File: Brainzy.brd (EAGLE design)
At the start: 100 x 80 mm, 46 parts, among them IC1 L293D, IC2 L293D

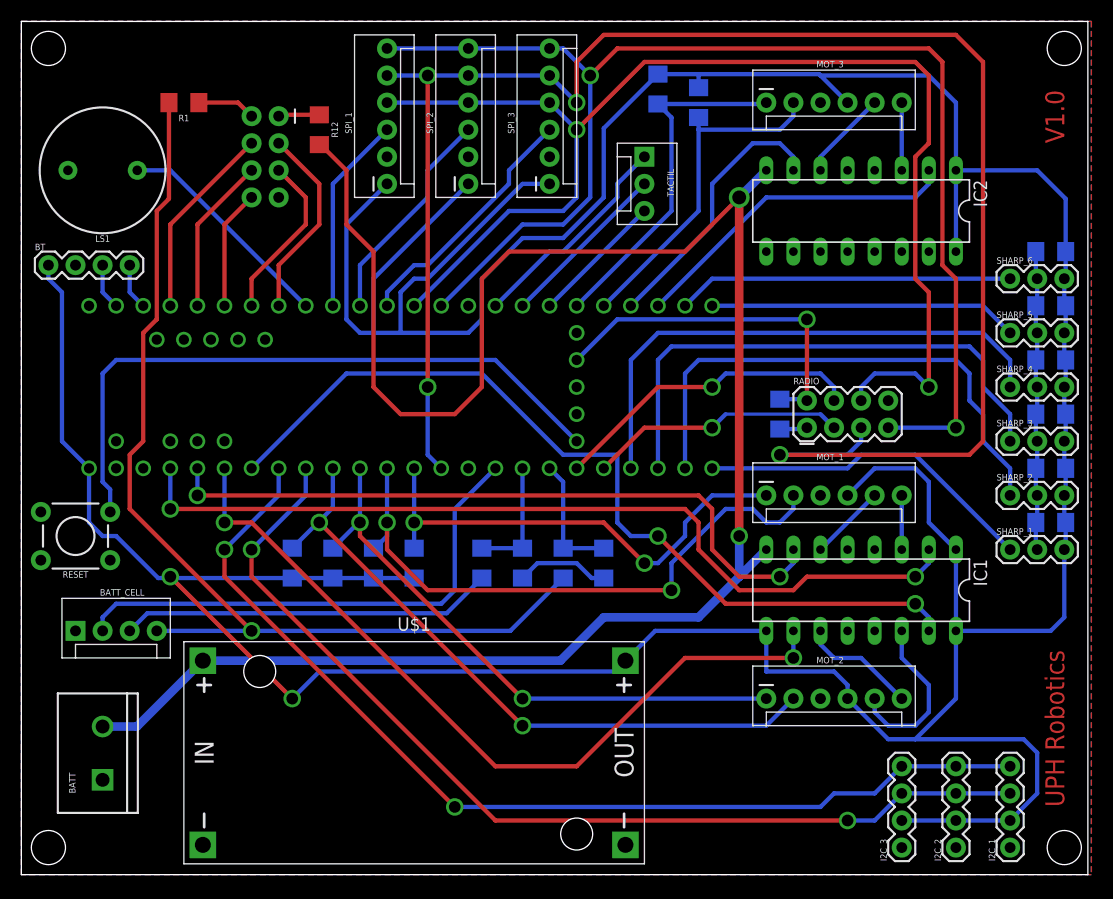
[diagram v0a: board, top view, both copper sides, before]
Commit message: Upload Brainzy v1.1
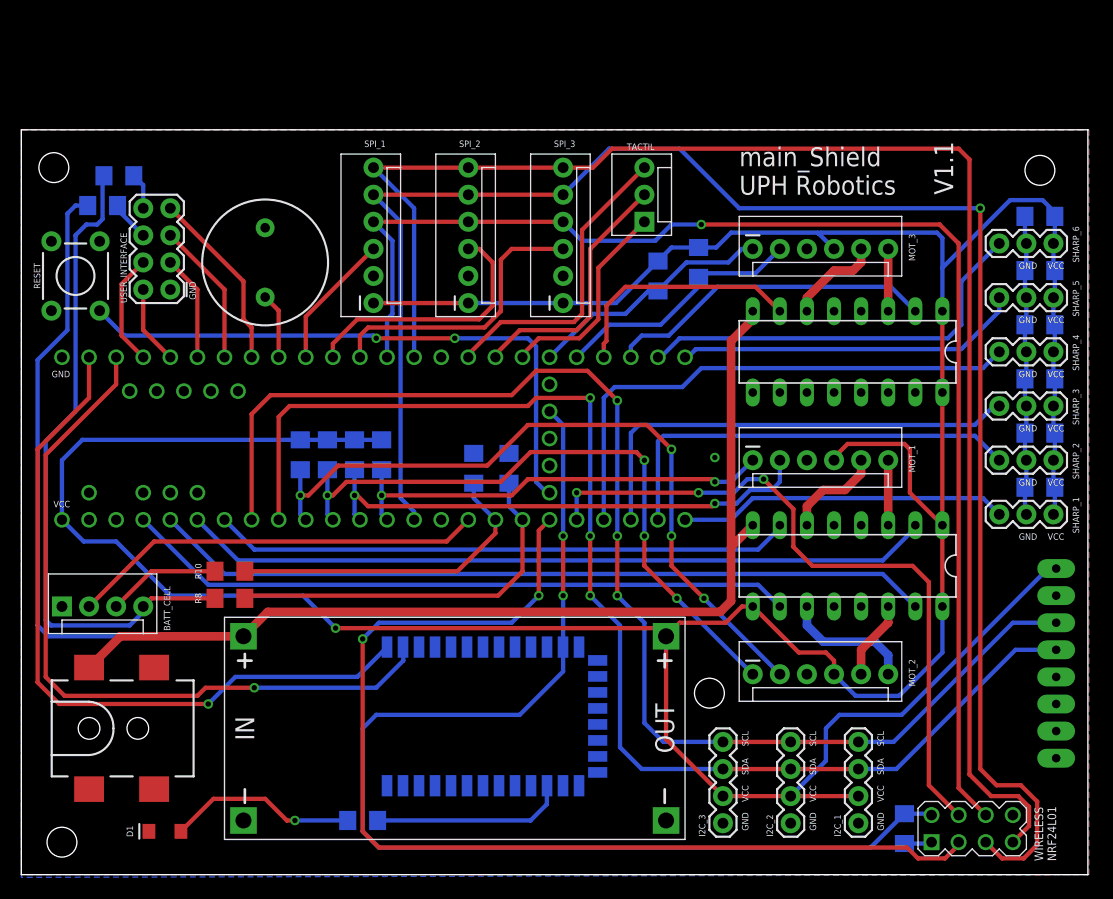
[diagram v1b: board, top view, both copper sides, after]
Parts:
- removed IU, RADIO: (no value), SparkFun-Connectors:2X4
- removed U$1: DC-DC-STEP-DOWN-LM2596, DC-DC-STEP-DOWN-LM2596:DC-DC-STEP-DOWN-LM2596
- added D1: (no value), SparkFun-LED:LED-1206
- added M1: WIRELESS-NRF24L01, diy-modules copy:WIRELESS-NRF24L01
- added POWER_CONVERTER: DC-DC-STEP-DOWN-LM2596, diy-modules copy:DC-DC-STEP-DOWN-LM2596
- added R13: 470, SparkFun-Resistors:1206
- added U1: GY-521MPU6050, gy-521:GY-521
- added USER_INTERFACE: (no value), SparkFun-Connectors:2X4
- BATT: value (none) -> 5.5x2.1mm Barrel; device SparkFun-Connectors:SCREWTERMINAL-5MM-2 -> SparkFun-Connectors:POWER_JACK_SMD
- BT: value (none) -> HC-06/HC_05; device SparkFun-Connectors:1X04 -> SerialPortBluetooth:BLUETOOTH_SMD
- TEENSY_3.2/3.5: value TEENSY_3.5_ALL_PINS -> TEENSY_ALL_PINS
- moved BT 47.9 mm to (34.3, 21.3), flipped to the bottom, turned to 270 degrees
- moved C1 40.6 mm to (82.8, 4.32), turned to 270 degrees
- moved R8 31.4 mm to (19.6, 25.9), flipped to the top, turned to 180 degrees
- moved RESET 24.4 mm to (5.08, 56.1), turned to 90 degrees
- moved R10 23.6 mm to (19.6, 28.4), flipped to the top, turned to 180 degrees
- moved R12 21.5 mm to (7.62, 62.7), flipped to the bottom, turned to 0 degrees
- moved R7 17.5 mm to (59.7, 56.1)
- moved LS1 17.5 mm to (22.9, 57.4), turned to 90 degrees
- moved I2C_3 16.9 mm to (65.8, 4.83)
- moved I2C_2 15.7 mm to (72.1, 4.83)
- moved R6 15.0 mm to (63.5, 57.4)
- moved I2C_1 14.4 mm to (78.5, 4.83)
- moved MOT_3 13.8 mm to (68.6, 58.7)
- moved IC2 13.3 mm to (77.5, 49.0)
- moved R9 12.6 mm to (45.7, 38.1), turned to 270 degrees
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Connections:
- removed net N$2: IU.2, R1.1
- new net N$3: D1.A, R13.1
- new net N$4: R12.1, USER_INTERFACE.6
- new net N$6: BT.24, R13.2
- net 12V: now also BATT.VIN0, POWER_CONVERTER.IN+; no longer BATT.2, U$1.IN+
- net 3.3V: now also BT.12, C1.1, M1.2; no longer C1.2, RADIO.2
- net 5V: now also POWER_CONVERTER.OUT+, U1.VCC; no longer BT.1, U$1.OUT+
- net BTN_CENTER: now also USER_INTERFACE.3; no longer IU.8
- net BTN_DOWN: now also USER_INTERFACE.7; no longer IU.3
- net BTN_LEFT: now also USER_INTERFACE.2; no longer IU.6
- net BTN_RIGHT: now also USER_INTERFACE.5; no longer IU.5
- net BTN_UP: now also USER_INTERFACE.4; no longer IU.4
- net BT_RX: now also BT.1; no longer BT.3
- net BT_TX: now also BT.2; no longer BT.4
- net GND: now also BATT.GND, BT.13, BT.21, BT.22, C1.2, D1.C, M1.1, POWER_CONVERTER.IN-, POWER_CONVERTER.OUT-, U1.GND, USER_INTERFACE.1; no longer BATT.1, BT.2, C1.1, IU.7, RADIO.1, U$1.IN-, U$1.OUT-
- net MOT1_1: now also TEENSY_3.2/3.5.21/A7; no longer TEENSY_3.2/3.5.23/A9
- net MOT1_2: now also TEENSY_3.2/3.5.20/A6; no longer TEENSY_3.2/3.5.22/A8
- net MOT2_1: now also TEENSY_3.2/3.5.23/A9; no longer TEENSY_3.2/3.5.21/A7
- net MOT2_2: now also TEENSY_3.2/3.5.22/A8; no longer TEENSY_3.2/3.5.20/A6
- net N$1: now also R1.1, USER_INTERFACE.8; no longer IU.1, R12.1
- net RADIO_CE: now also M1.3, TEENSY_3.2/3.5.38/A19; no longer RADIO.3, TEENSY_3.2/3.5.37/A18
- net RADIO_CS: now also M1.4, TEENSY_3.2/3.5.37/A18; no longer RADIO.4, TEENSY_3.2/3.5.38/A19
- net SCL: now also U1.SCL
- net SDA: now also U1.SDA
- net SPI_MISO: now also M1.7; no longer RADIO.7
- net SPI_MOSI: now also M1.6; no longer RADIO.6
- net SPI_SCK: now also M1.5; no longer RADIO.5
- net T_CS2: now also TACTIL.1; no longer TACTIL.3
- net T_IRQ: now also TACTIL.3; no longer TACTIL.1
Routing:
- net 3.3V: track 33.4 -> 110.9 mm, vias 1 -> 2
- net RADIO_CE: track 24.2 -> 101.5 mm, vias 1 -> 2
- net 5V: track 417.8 -> 352.2 mm, vias 2 -> 1
- net BT_TX: track 4.34 -> 69.6 mm, vias 0 -> 1
- net BT_RX: track 4.34 -> 68.3 mm, vias 0 -> 1
- net RADIO_CS: track 29.6 -> 65.2 mm, vias 1 -> 3
- net VDD: track 95.9 -> 61.9 mm, vias 1 -> 0
- net 12V: track 182.9 -> 155.4 mm, vias 2 -> 0
- net SDA: track 93.9 -> 119.9 mm, vias 2 -> 3
- net SCL: track 96.4 -> 122.3 mm, vias 2 -> 3
- net N$5: track 35.1 -> 10.6 mm
- net CELL3: track 11.8 -> 35.9 mm
- net SPI_MISO: track 125.5 -> 144.8 mm, vias 2 -> 0
- net CELL2: track 11.3 -> 30.5 mm
- net N$6: track 0.00 -> 18.2 mm
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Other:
- board size 100 x 80 mm -> 100 x 69.8 mm
- board text added: "GND"
- board text added: "SCL"
- board text added: "SDA"
- board text added: "V1.1"
- board text added: "VCC"
- board text added: "WIRELESS NRF24L01"
- board text added: "main_Shield UPH Robotics"
- board text removed: "UPH Robotics"
- board text removed: "V1.0"
